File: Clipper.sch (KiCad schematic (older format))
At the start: 34 parts, among them U15 LME49740, U16 LME49740

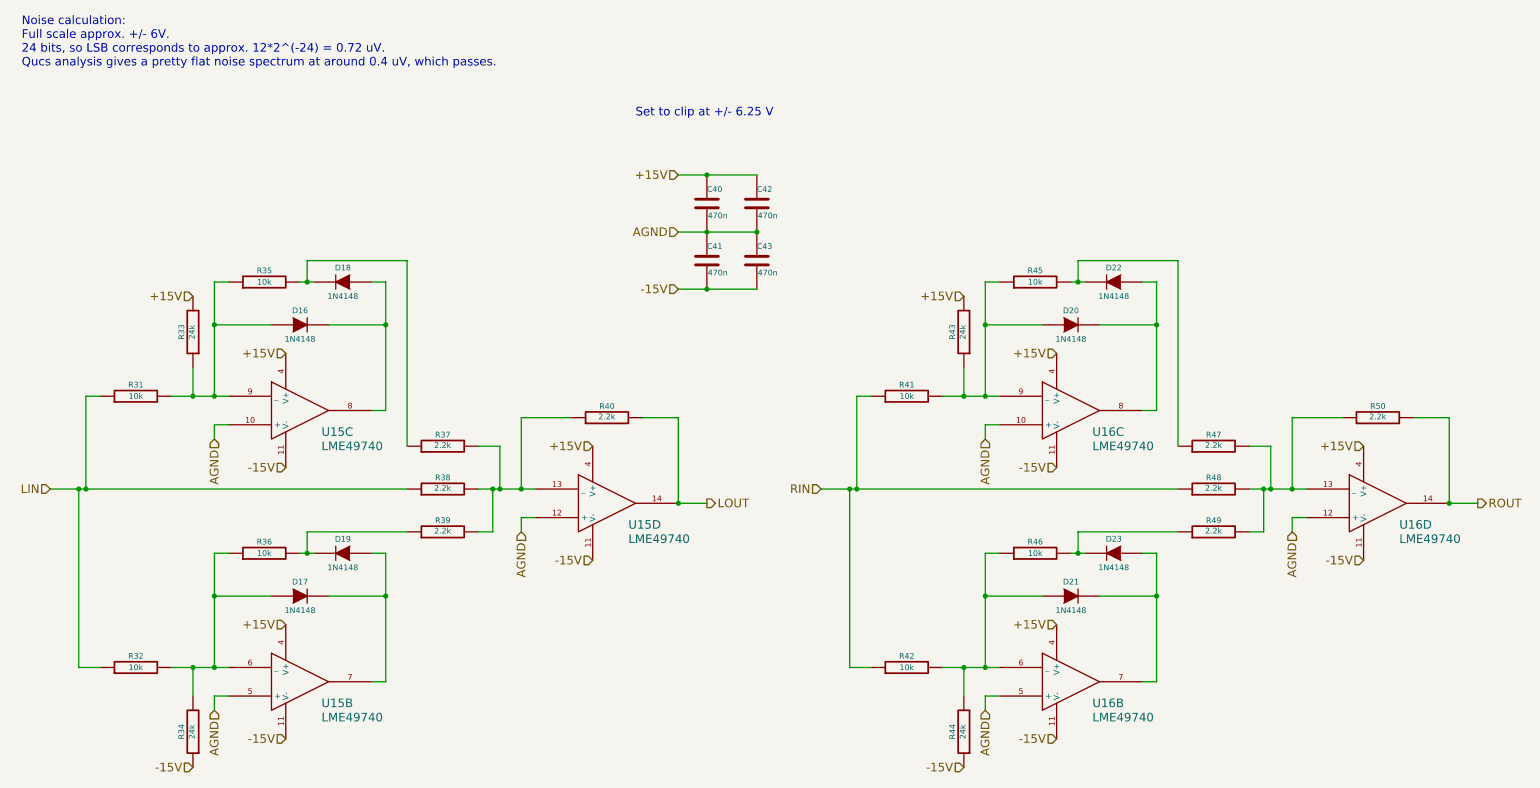
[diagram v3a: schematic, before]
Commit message: A lot of routing, some parts changes:   * Added snubber C/RC snubbers to transformer secondaries.   * Changed PSU OA from OPA209 to OPA27.   * Routed external PSU.   * Mostly done routing internal circuits.  Just need to get everything together.   * Changed digital transformer to a more appropriately-specced one.
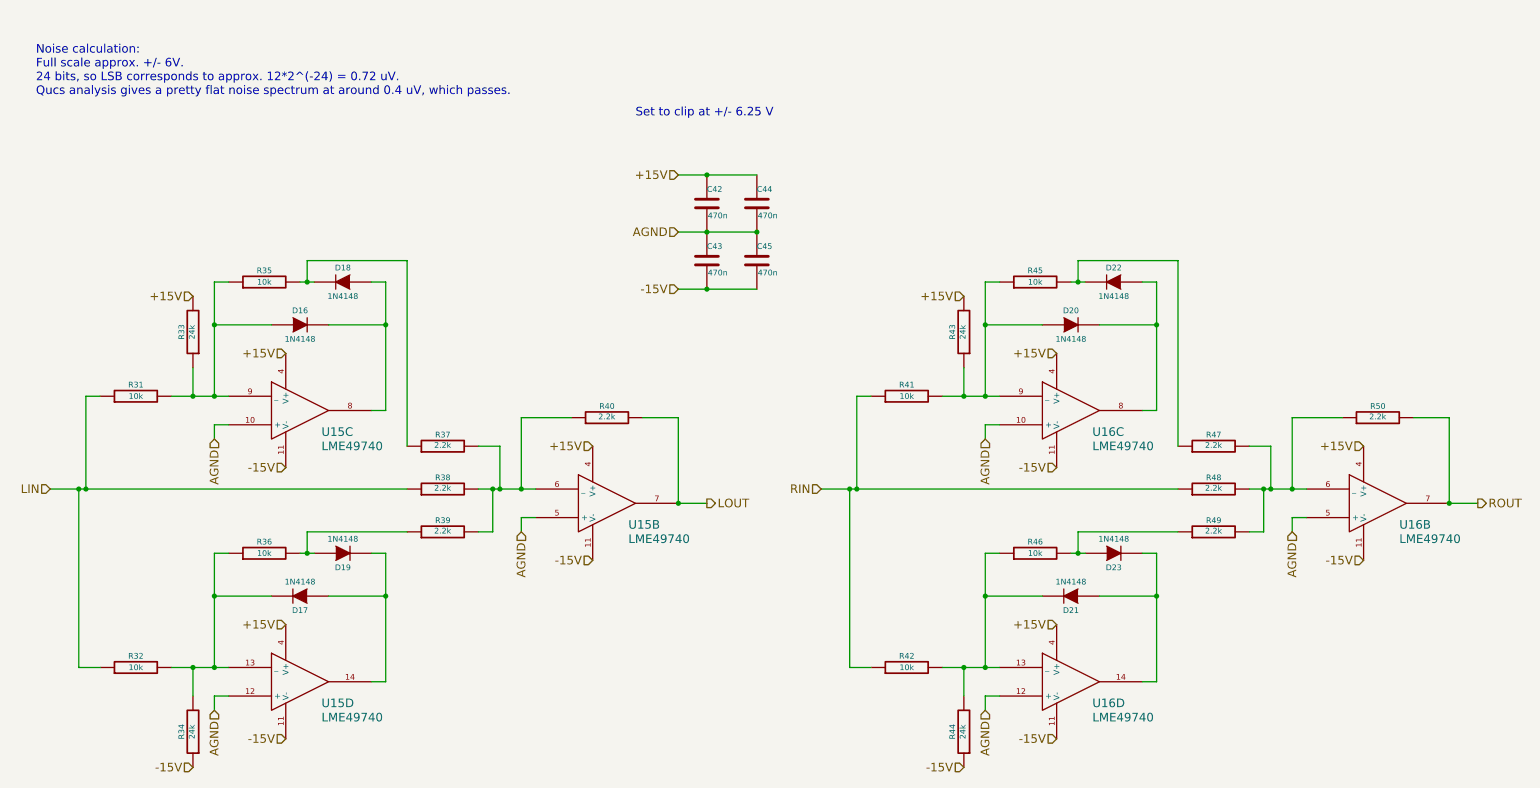
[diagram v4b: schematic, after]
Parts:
- renumbered C40 to C42, C41 to C43, C42 to C44, C43 to C45
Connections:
- net AGND: now also U15.12 (+), U15.5 (+), U16.12 (+), U16.5 (+); no longer U15.12 (+), U15.5 (+), U16.12 (+), U16.5 (+)
- net LOUT: now also U15.7; no longer U15.14
- net ROUT: now also U16.7; no longer U16.14
- net at R32.2, R34.2, R36.1: now also D17.2 (K), U15.13 (_); no longer D17.1 (A), U15.6 (_)
- net at R36.2, R39.1: now also D19.1 (A); no longer D19.2 (K)
- net at R42.2, R44.2, R46.1: now also D21.2 (K), U16.13 (_); no longer D21.1 (A), U16.6 (_)
- net at R46.2, R49.1: now also D23.1 (A); no longer D23.2 (K)
- net at R47.2, R48.2, R49.2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: now also U16.6 (_); no longer U16.13 (_)
- net at R37.2, R38.2, R39.2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: now also U15.6 (_); no longer U15.13 (_)
- new net: D17.1 (A), D19.2 (K), U15.14
- new net: D21.1 (A), D23.2 (K), U16.14
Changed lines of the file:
@@
 F 4 "568-1360-1-ND" H 2600 4450 60  0001 C CNN "DigiKey"
 	1    2600 4450
-	1    0    0    -1
+	-1   0    0    1
 $EndComp
 $Comp
@@
 F 4 "568-1360-1-ND" H 2900 4150 60  0001 C CNN "DigiKey"
 	1    2900 4150
-	-1   0    0    -1
+	1    0    0    1
 $EndComp
 Text HLabel 1850 5650 0    60   Input ~ 0
@@
 F 4 "568-1360-1-ND" H 8000 4450 60  0001 C CNN "DigiKey"
 	1    8000 4450
-	1    0    0    -1
+	-1   0    0    1
 $EndComp
 $Comp
@@
 F 4 "568-1360-1-ND" H 8300 4150 60  0001 C CNN "DigiKey"
 	1    8300 4150
-	-1   0    0    -1
+	1    0    0    1
 $EndComp
 Text HLabel 7250 5650 0    60   Input ~ 0
@@
 Set to clip at +/- 6.25 V
 $Comp
-L C C40
+L C C42
 U 1 1 536EC1E0
 P 5450 1700
-F 0 "C40" H 5450 1800 40  0000 L CNN
+F 0 "C42" H 5450 1800 40  0000 L CNN
 F 1 "470n" H 5456 1615 40  0000 L CNN
 F 2 "Capacitors_ThroughHole:Capacitor3MMDiscRM2.5" H 5488 1550 30  0001 C CNN
@@
 Wire Wire Line
 	9350 3700 9350 4000
-Text Notes 650  750  0    60   ~ 0
+Text Notes 750  950  0    60   ~ 0
 Noise calculation:\nFull scale approx. +/- 6V.\n24 bits, so LSB corresponds to approx. 12*2^(-24) = 0.72 uV.\nQucs analysis gives a pretty flat noise spectrum at around 0.4 uV, which passes.
 $Comp
@@
 $EndComp
 $Comp
-L C C42
+L C C44
 U 1 1 537D7769
 P 5800 1700
-F 0 "C42" H 5800 1800 40  0000 L CNN
+F 0 "C44" H 5800 1800 40  0000 L CNN
 F 1 "470n" H 5806 1615 40  0000 L CNN
 F 2 "Capacitors_ThroughHole:Capacitor3MMDiscRM2.5" H 5838 1550 30  0001 C CNN
@@
 $EndComp
 $Comp
-L C C41
+L C C43
 U 1 1 537D7778
 P 5450 2100
-F 0 "C41" H 5450 2200 40  0000 L CNN
+F 0 "C43" H 5450 2200 40  0000 L CNN
 F 1 "470n" H 5456 2015 40  0000 L CNN
 F 2 "Capacitors_ThroughHole:Capacitor3MMDiscRM2.5" H 5488 1950 30  0001 C CNN
@@
 $EndComp
 $Comp
-L C C43
+L C C45
 U 1 1 537D7787
 P 5800 2100
-F 0 "C43" H 5800 2200 40  0000 L CNN
+F 0 "C45" H 5800 2200 40  0000 L CNN
 F 1 "470n" H 5806 2015 40  0000 L CNN
 F 2 "Capacitors_ThroughHole:Capacitor3MMDiscRM2.5" H 5838 1950 30  0001 C CNN
@@
 $Comp
 L LME49740 U15
-U 2 1 53803307
+U 4 1 53803307
 P 2500 5050
 F 0 "U15" H 2750 4900 60  0000 L CNN
@@
 F 2 "Sockets_DIP:DIP-14__300_ELL" H 2600 5050 60  0001 C CNN
 F 3 "~" H 2600 5050 60  0000 C CNN
-	2    2500 5050
+	4    2500 5050
 	1    0    0    -1
 $EndComp
 $Comp
 L LME49740 U16
-U 2 1 53803335
+U 4 1 53803335
 P 7900 5050
 F 0 "U16" H 8150 4900 60  0000 L CNN
@@
 F 2 "Sockets_DIP:DIP-14__300_ELL" H 8000 5050 60  0001 C CNN
 F 3 "~" H 8000 5050 60  0000 C CNN
-	2    7900 5050
+	4    7900 5050
 	1    0    0    -1
 $EndComp
@@
 $Comp
 L LME49740 U15
-U 4 1 538036F5
+U 2 1 538036F5
 P 4650 3800
 F 0 "U15" H 4900 3650 60  0000 L CNN
@@
 F 2 "Sockets_DIP:DIP-14__300_ELL" H 4750 3800 60  0001 C CNN
 F 3 "~" H 4750 3800 60  0000 C CNN
-	4    4650 3800
+	2    4650 3800
 	1    0    0    -1
 $EndComp
 $Comp
 L LME49740 U16
-U 4 1 5380372A
+U 2 1 5380372A
 P 10050 3800
 F 0 "U16" H 10300 3650 60  0000 L CNN
@@
 F 2 "Sockets_DIP:DIP-14__300_ELL" H 10150 3800 60  0001 C CNN
 F 3 "~" H 10150 3800 60  0000 C CNN
-	4    10050 3800
-	1    0    0    -1
-$EndComp
+	2    10050 3800
+	1    0    0    -1
+$EndComp
